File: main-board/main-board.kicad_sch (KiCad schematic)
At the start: 52 parts, among them J4 Conn_01x03_Pin, J5 COM, J6 Conn_01x03_Pin, SW1 SW_SPST, U1 ADA4898-2, U2 ADA4898-2, U3 AD633ANZ

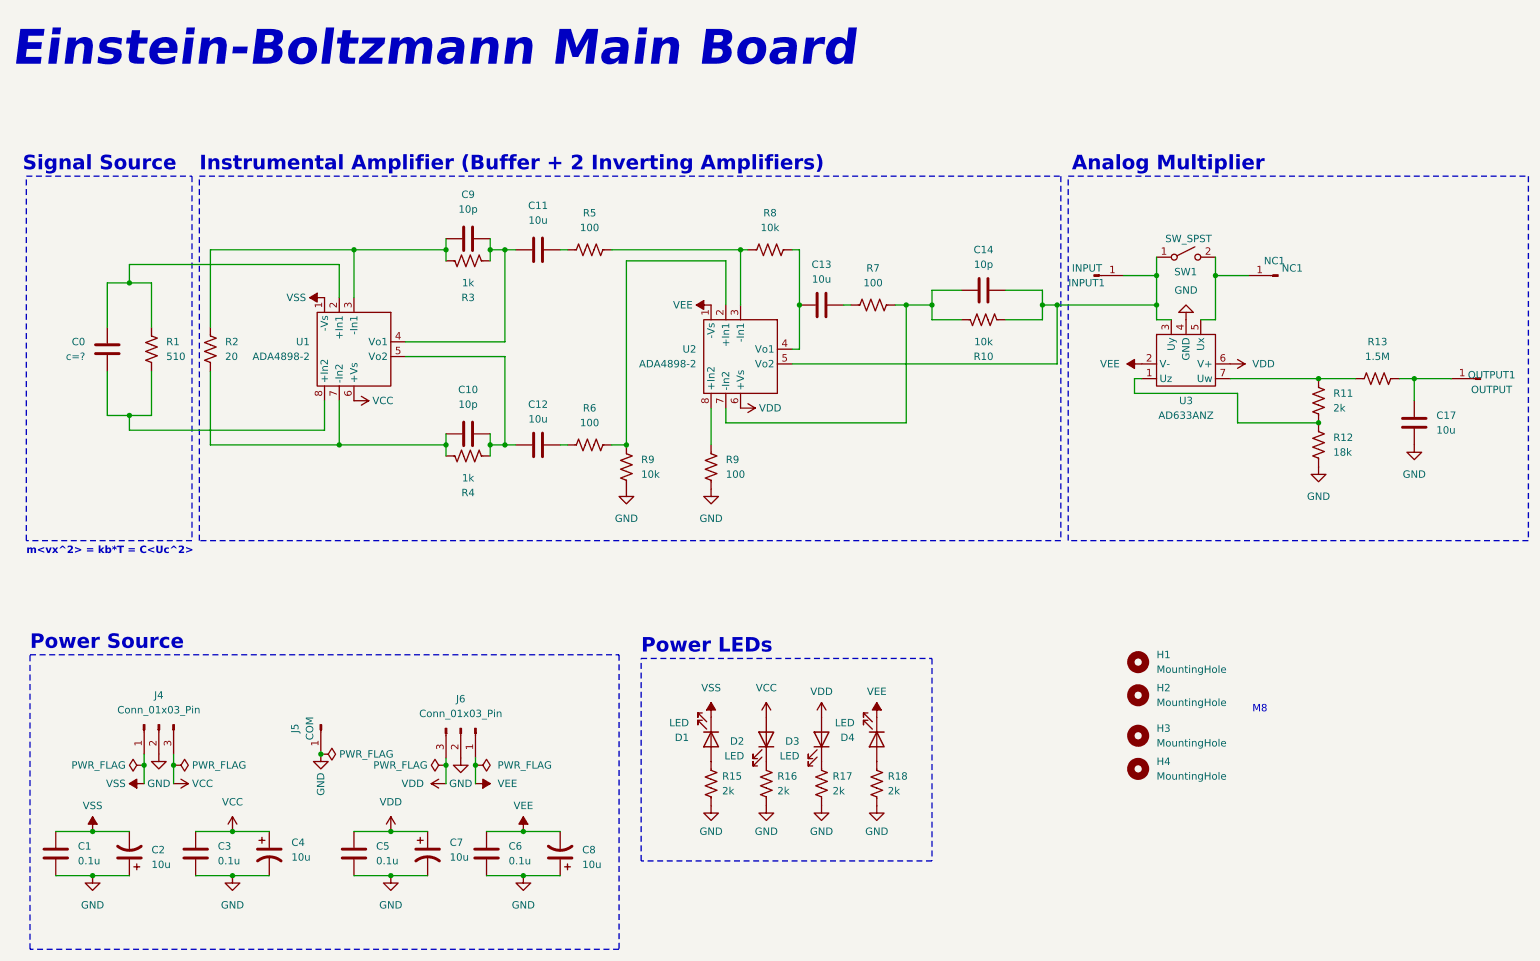
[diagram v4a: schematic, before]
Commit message: Modifies Main Board PCB Layout component disposal
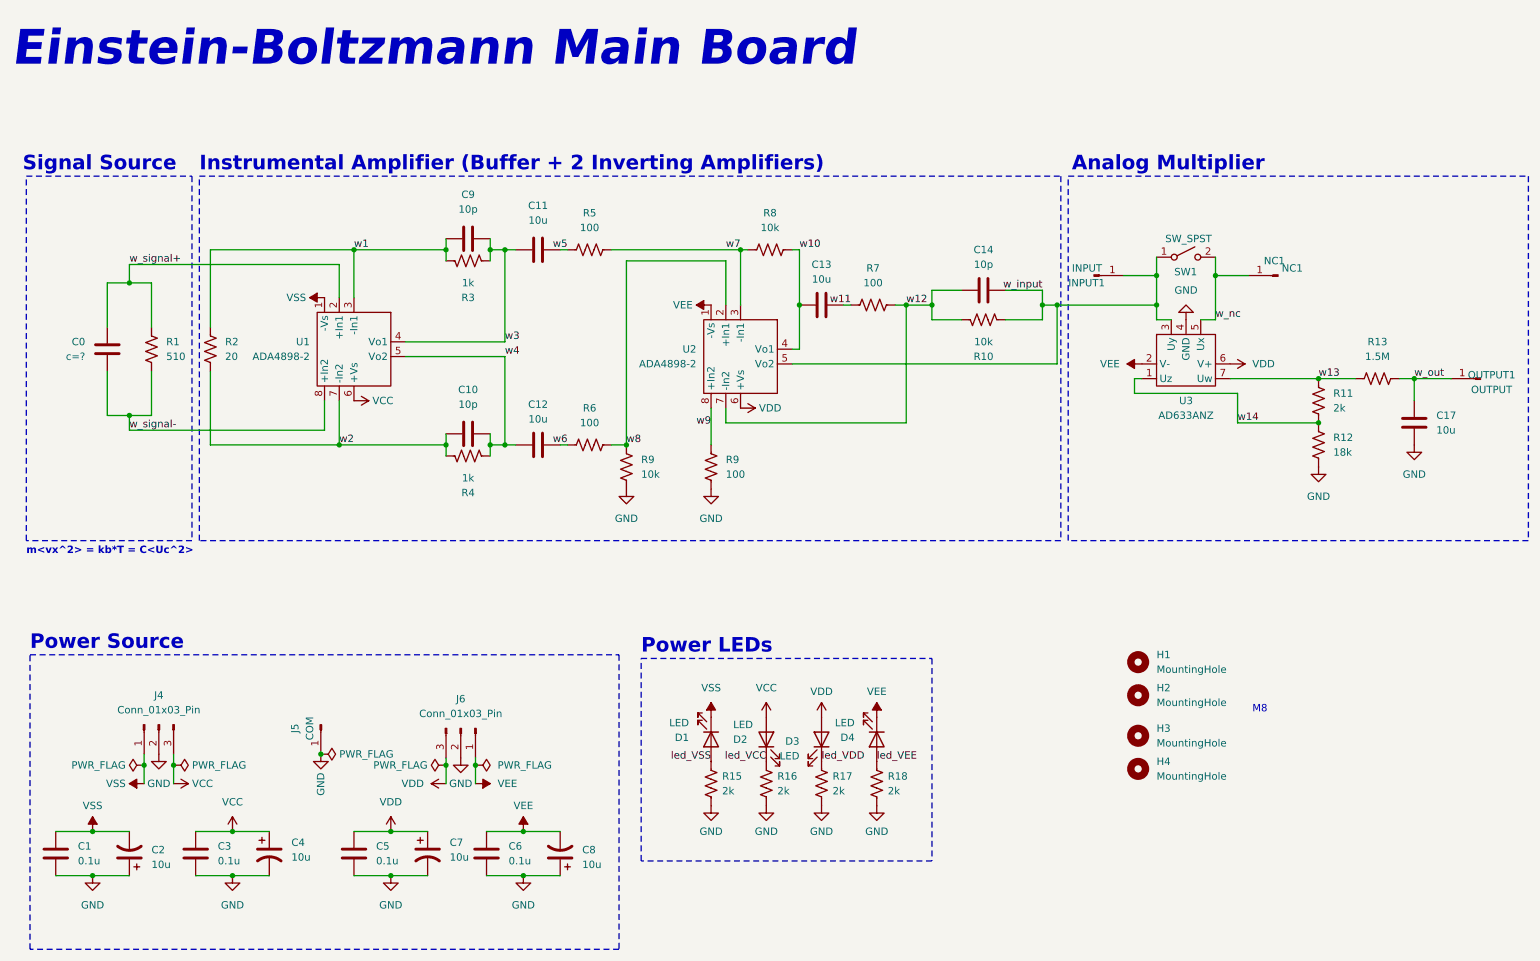
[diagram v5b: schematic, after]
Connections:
- net w_signal-: now reaches C0.1, R1.2, U1.8 (+In2)
- net w_signal+: now reaches C0.2, R1.1, U1.2 (+In1)
- net w5: now reaches C11.2, R5.1
- net w7: now reaches R5.2, R8.1, U2.3 (-In1)
- net w12: now reaches C14.1, R10.1, R7.2, U2.7 (-In2)
- net w_input: now reaches C14.2, INPUT1.1 (Pin_1), R10.2, SW1.1 (A), U2.5 (Vo2), U3.3 (Uy)
- net w10: now reaches C13.1, R8.2, U2.4 (Vo1)
- net w11: now reaches C13.2, R7.1
- net w4: now reaches C10.2, C12.1, R4.1, U1.5 (Vo2)
- net w2: now reaches C10.1, R2.2, R4.2, U1.7 (-In2)
- net led_VDD: now reaches D3.1 (K), R17.1
- net w1: now reaches C9.1, R2.1, R3.1, U1.3 (-In1)
- net w3: now reaches C11.1, C9.2, R3.2, U1.4 (Vo1)
- net w9: now reaches R9.2, U2.8 (+In2)
- net led_VSS: now reaches D1.2 (A), R15.1
- net w_nc: now reaches NC1.1 (Pin_1), SW1.2 (B), U3.5 (Ux)
- net w6: now reaches C12.2, R6.1
- net w8: now reaches R6.2, R9.2, U2.2 (+In1)
- net w14: now reaches R11.2, R12.1, U3.1 (Uz)
- net w_out: now reaches C17.1, OUTPUT1.1 (Pin_1), R13.2
- net led_VCC: now reaches D2.1 (K), R16.1
- net w13: now reaches R11.1, R13.1, U3.7 (Uw)
- net led_VEE: now reaches D4.2 (A), R18.1
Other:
- moved on the sheet: D2
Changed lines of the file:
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@@
     (effects (font (size 2.5 2.5) bold) (justify left bottom))
+  )
+  (label "w_input" (at 196.215 65.405 180) (fields_autoplaced)
+    (effects (font (size 1.27 1.27)) (justify right bottom))
+  )
+  (label "w_out" (at 260.35 80.645 0) (fields_autoplaced)
+    (effects (font (size 1.27 1.27)) (justify left bottom))
+  )
+  (label "w8" (at 124.46 92.075 0) (fields_autoplaced)
+    (effects (font (size 1.27 1.27)) (justify left bottom))
+  )
+  (label "led_VCC" (at 148.59 146.685 180) (fields_autoplaced)
+    (effects (font (size 1.27 1.27)) (justify right bottom))
+  )
+  (label "w6" (at 114.3 92.075 180) (fields_autoplaced)
+    (effects (font (size 1.27 1.27)) (justify right bottom))
+  )
+  (label "w3" (at 103.505 74.295 0) (fields_autoplaced)
+    (effects (font (size 1.27 1.27)) (justify left bottom))
+  )
+  (label "w14" (at 229.87 88.265 0) (fields_autoplaced)
+    (effects (font (size 1.27 1.27)) (justify left bottom))
+  )
+  (label "w_nc" (at 226.06 70.485 0) (fields_autoplaced)
+    (effects (font (size 1.27 1.27)) (justify left bottom))
+  )
+  (label "led_VSS" (at 139.065 146.685 180) (fields_autoplaced)
+    (effects (font (size 1.27 1.27)) (justify right bottom))
+  )
+  (label "w1" (at 77.47 58.42 0) (fields_autoplaced)
+    (effects (font (size 1.27 1.27)) (justify left bottom))
+  )
+  (label "w4" (at 103.505 76.835 0) (fields_autoplaced)
+    (effects (font (size 1.27 1.27)) (justify left bottom))
+  )
+  (label "led_VEE" (at 167.64 146.685 0) (fields_autoplaced)
+    (effects (font (size 1.27 1.27)) (justify left bottom))
+  )
+  (label "w7" (at 144.145 58.42 180) (fields_autoplaced)
+    (effects (font (size 1.27 1.27)) (justify right bottom))
+  )
+  (label "w5" (at 114.3 58.42 180) (fields_autoplaced)
+    (effects (font (size 1.27 1.27)) (justify right bottom))
+  )
+  (label "w13" (at 243.84 80.645 0) (fields_autoplaced)
+    (effects (font (size 1.27 1.27)) (justify left bottom))
+  )
+  (label "w10" (at 154.305 58.42 0) (fields_autoplaced)
+    (effects (font (size 1.27 1.27)) (justify left bottom))
+  )
+  (label "w11" (at 163.195 67.945 180) (fields_autoplaced)
+    (effects (font (size 1.27 1.27)) (justify right bottom))
+  )
+  (label "w_signal+" (at 38.735 60.96 0) (fields_autoplaced)
+    (effects (font (size 1.27 1.27)) (justify left bottom))
+  )
+  (label "w9" (at 139.065 88.9 180) (fields_autoplaced)
+    (effects (font (size 1.27 1.27)) (justify right bottom))
+  )
+  (label "w_signal-" (at 38.735 89.535 0) (fields_autoplaced)
+    (effects (font (size 1.27 1.27)) (justify left bottom))
+  )
+  (label "w12" (at 172.72 67.945 0) (fields_autoplaced)
+    (effects (font (size 1.27 1.27)) (justify left bottom))
+  )
+  (label "led_VDD" (at 158.115 146.685 0) (fields_autoplaced)
+    (effects (font (size 1.27 1.27)) (justify left bottom))
+  )
+  (label "w2" (at 74.93 92.075 0) (fields_autoplaced)
+    (effects (font (size 1.27 1.27)) (justify left bottom))
   )
   (symbol (lib_id "Device:C") (at 34.925 75.565 0) (mirror x) (unit 1)
@@
     )
   )
-  (symbol (lib_id "Device:LED") (at 148.59 142.875 270) (mirror x) (unit 1)
+  (symbol (lib_id "Device:LED") (at 148.59 142.875 90) (unit 1)
     (in_bom yes) (on_board yes) (dnp no)
-    (property "Reference" "D2" (at 144.78 143.1925 90)
-      (effects (font (size 1.27 1.27)) (justify right))
-    )
-    (property "Value" "LED" (at 144.78 145.7325 90)
-      (effects (font (size 1.27 1.27)) (justify right))
-    )
+    (property "Reference" "D2" (at 142.875 142.875 90)
+      (effects (font (size 1.27 1.27)) (justify right))
+    )
+    (property "Value" "LED" (at 142.875 140.335 90)
+      (effects (font (size 1.27 1.27)) (justify right))
+    )

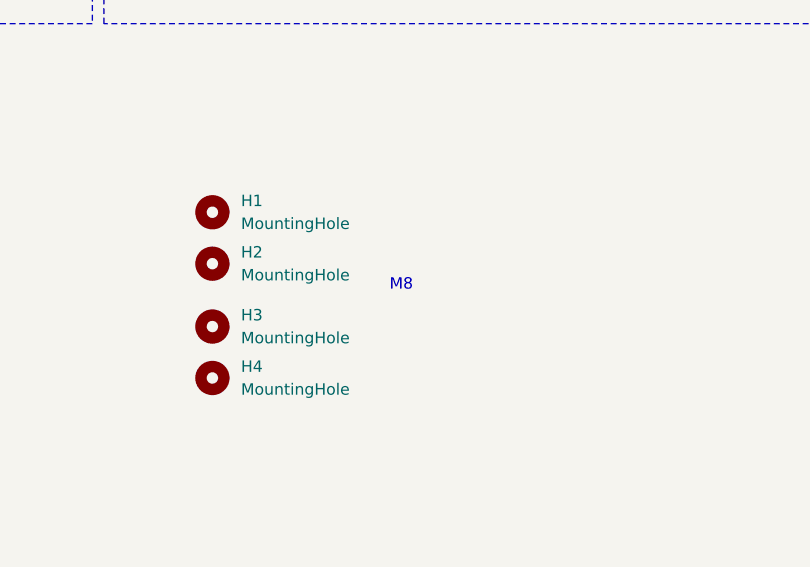
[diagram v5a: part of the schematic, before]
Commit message: Change M8 Holes to M5 Holes
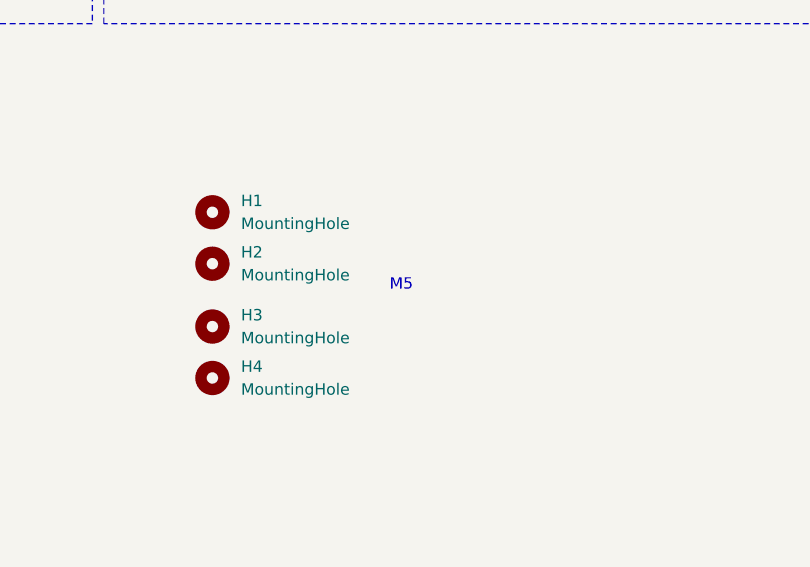
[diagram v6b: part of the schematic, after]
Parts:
- H1, H2, H3, H4: footprint MountingHole:MountingHole_8.4mm_M8 -> MountingHole:MountingHole_5.3mm_M5
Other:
- note added: "M5"
- note removed: "M8"
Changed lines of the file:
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@@
     (effects (font (size 2.5 2.5) bold) (justify left bottom))
   )
-  (text "M8" (at 232.41 138.43 0)
+  (text "M5" (at 232.41 138.43 0)
     (effects (font (size 1.27 1.27)) (justify left bottom))
   )
@@
       (effects (font (size 1.27 1.27)) (justify left))
     )
-    (property "Footprint" "MountingHole:MountingHole_8.4mm_M8" (at 212.725 129.54 0)
+    (property "Footprint" "MountingHole:MountingHole_5.3mm_M5" (at 212.725 129.54 0)
       (effects (font (size 1.27 1.27)) hide)
     )
@@
       (effects (font (size 1.27 1.27)) (justify left))
     )
-    (property "Footprint" "MountingHole:MountingHole_8.4mm_M8" (at 212.725 142.24 0)
+    (property "Footprint" "MountingHole:MountingHole_5.3mm_M5" (at 212.725 142.24 0)
       (effects (font (size 1.27 1.27)) hide)
     )
@@
       (effects (font (size 1.27 1.27)) (justify left))
     )
-    (property "Footprint" "MountingHole:MountingHole_8.4mm_M8" (at 212.725 135.255 0)
+    (property "Footprint" "MountingHole:MountingHole_5.3mm_M5" (at 212.725 135.255 0)
       (effects (font (size 1.27 1.27)) hide)
     )
@@
       (effects (font (size 1.27 1.27)) (justify left))
     )
-    (property "Footprint" "MountingHole:MountingHole_8.4mm_M8" (at 212.725 147.955 0)
-      (effects (font (size 1.27 1.27)) hide)
-    )
+    (property "Footprint" "MountingHole:MountingHole_5.3mm_M5" (at 212.725 147.955 0)
+      (effects (font (size 1.27 1.27)) hide)
+    )

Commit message: Changes capacitor and resistor footprints
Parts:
- C11, C12, C13, C17: footprint Capacitor_THT:C_Disc_D6.0mm_W2.5mm_P5.00mm -> Capacitor_THT:C_Rect_L24.0mm_W8.6mm_P22.50mm_MKT
- R1, R10, R11, R12, R13, R15, R16, R17, R18, R2, R3, R4, R5, R6, R7, R8, R9: footprint Resistor_THT:R_Axial_DIN0207_L6.3mm_D2.5mm_P15.24mm_Horizontal -> Resistor_THT:R_Axial_DIN0207_L6.3mm_D2.5mm_P7.62mm_Horizontal
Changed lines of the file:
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@@
       (effects (font (size 1.27 1.27)))
     )
-    (property "Footprint" "Resistor_THT:R_Axial_DIN0207_L6.3mm_D2.5mm_P15.24mm_Horizontal" (at 118.364 57.404 90)
+    (property "Footprint" "Resistor_THT:R_Axial_DIN0207_L6.3mm_D2.5mm_P7.62mm_Horizontal" (at 118.364 57.404 90)
       (effects (font (size 1.27 1.27)) hide)
     )
@@
       (effects (font (size 1.27 1.27)))
     )
-    (property "Footprint" "Capacitor_THT:C_Disc_D6.0mm_W2.5mm_P5.00mm" (at 161.925 66.9798 0)
+    (property "Footprint" "Capacitor_THT:C_Rect_L24.0mm_W8.6mm_P22.50mm_MKT" (at 161.925 66.9798 0)
       (effects (font (size 1.27 1.27)) hide)
     )
@@
       (effects (font (size 1.27 1.27)))
     )
-    (property "Footprint" "Resistor_THT:R_Axial_DIN0207_L6.3mm_D2.5mm_P15.24mm_Horizontal" (at 96.901 92.964 90)
+    (property "Footprint" "Resistor_THT:R_Axial_DIN0207_L6.3mm_D2.5mm_P7.62mm_Horizontal" (at 96.901 92.964 90)
       (effects (font (size 1.27 1.27)) hide)
     )
@@
       (effects (font (size 1.27 1.27)))
     )
-    (property "Footprint" "Resistor_THT:R_Axial_DIN0207_L6.3mm_D2.5mm_P15.24mm_Horizontal" (at 186.309 71.501 90)
+    (property "Footprint" "Resistor_THT:R_Axial_DIN0207_L6.3mm_D2.5mm_P7.62mm_Horizontal" (at 186.309 71.501 90)
       (effects (font (size 1.27 1.27)) hide)
     )
@@
       (effects (font (size 1.27 1.27)))
     )
-    (property "Footprint" "Capacitor_THT:C_Disc_D6.0mm_W2.5mm_P5.00mm" (at 113.03 57.4548 0)
+    (property "Footprint" "Capacitor_THT:C_Rect_L24.0mm_W8.6mm_P22.50mm_MKT" (at 113.03 57.4548 0)
       (effects (font (size 1.27 1.27)) hide)
     )
@@
       (effects (font (size 1.27 1.27)) (justify right))
     )
-    (property "Footprint" "Resistor_THT:R_Axial_DIN0207_L6.3mm_D2.5mm_P15.24mm_Horizontal" (at 138.049 95.631 90)
+    (property "Footprint" "Resistor_THT:R_Axial_DIN0207_L6.3mm_D2.5mm_P7.62mm_Horizontal" (at 138.049 95.631 90)
       (effects (font (size 1.27 1.27)) hide)
     )
@@
       (effects (font (size 1.27 1.27)))
     )
-    (property "Footprint" "Capacitor_THT:C_Disc_D6.0mm_W2.5mm_P5.00mm" (at 113.03 91.1098 0)
+    (property "Footprint" "Capacitor_THT:C_Rect_L24.0mm_W8.6mm_P22.50mm_MKT" (at 113.03 91.1098 0)
       (effects (font (size 1.27 1.27)) hide)
     )
@@
       (effects (font (size 1.27 1.27)))
     )
-    (property "Footprint" "Resistor_THT:R_Axial_DIN0207_L6.3mm_D2.5mm_P15.24mm_Horizontal" (at 118.364 91.059 90)
+    (property "Footprint" "Resistor_THT:R_Axial_DIN0207_L6.3mm_D2.5mm_P7.62mm_Horizontal" (at 118.364 91.059 90)
       (effects (font (size 1.27 1.27)) hide)
     )
@@
       (effects (font (size 1.27 1.27)))
     )
-    (property "Footprint" "Resistor_THT:R_Axial_DIN0207_L6.3mm_D2.5mm_P15.24mm_Horizontal" (at 167.259 66.929 90)
+    (property "Footprint" "Resistor_THT:R_Axial_DIN0207_L6.3mm_D2.5mm_P7.62mm_Horizontal" (at 167.259 66.929 90)
       (effects (font (size 1.27 1.27)) hide)
     )
@@
       (effects (font (size 1.27 1.27)) (justify left))
     )
-    (property "Footprint" "Resistor_THT:R_Axial_DIN0207_L6.3mm_D2.5mm_P15.24mm_Horizontal" (at 244.856 92.329 90)
+    (property "Footprint" "Resistor_THT:R_Axial_DIN0207_L6.3mm_D2.5mm_P7.62mm_Horizontal" (at 244.856 92.329 90)
       (effects (font (size 1.27 1.27)) hide)
     )
@@
       (effects (font (size 1.27 1.27)) (justify left))
     )
-    (property "Footprint" "Capacitor_THT:C_Disc_D6.0mm_W2.5mm_P5.00mm" (at 261.3152 92.075 0)
+    (property "Footprint" "Capacitor_THT:C_Rect_L24.0mm_W8.6mm_P22.50mm_MKT" (at 261.3152 92.075 0)
       (effects (font (size 1.27 1.27)) hide)
     )
@@
       (effects (font (size 1.27 1.27)) (justify left))
     )
-    (property "Footprint" "Resistor_THT:R_Axial_DIN0207_L6.3mm_D2.5mm_P15.24mm_Horizontal" (at 244.856 84.709 90)
+    (property "Footprint" "Resistor_THT:R_Axial_DIN0207_L6.3mm_D2.5mm_P7.62mm_Horizontal" (at 244.856 84.709 90)
       (effects (font (size 1.27 1.27)) hide)
     )
@@
       (effects (font (size 1.27 1.27)) (justify left))
     )
-    (property "Footprint" "Resistor_THT:R_Axial_DIN0207_L6.3mm_D2.5mm_P15.24mm_Horizontal" (at 149.606 150.749 90)
+    (property "Footprint" "Resistor_THT:R_Axial_DIN0207_L6.3mm_D2.5mm_P7.62mm_Horizontal" (at 149.606 150.749 90)
       (effects (font (size 1.27 1.27)) hide)
     )
@@
       (effects (font (size 1.27 1.27)) (justify left))
     )
-    (property "Footprint" "Resistor_THT:R_Axial_DIN0207_L6.3mm_D2.5mm_P15.24mm_Horizontal" (at 168.656 150.749 90)
+    (property "Footprint" "Resistor_THT:R_Axial_DIN0207_L6.3mm_D2.5mm_P7.62mm_Horizontal" (at 168.656 150.749 90)
       (effects (font (size 1.27 1.27)) hide)
     )
@@
       (effects (font (size 1.27 1.27)))
     )
-    (property "Footprint" "Resistor_THT:R_Axial_DIN0207_L6.3mm_D2.5mm_P15.24mm_Horizontal" (at 254.254 79.629 90)
+    (property "Footprint" "Resistor_THT:R_Axial_DIN0207_L6.3mm_D2.5mm_P7.62mm_Horizontal" (at 254.254 79.629 90)
       (effects (font (size 1.27 1.27)) hide)
     )
@@
       (effects (font (size 1.27 1.27)) (justify left))
     )
-    (property "Footprint" "Resistor_THT:R_Axial_DIN0207_L6.3mm_D2.5mm_P15.24mm_Horizontal" (at 159.131 150.749 90)
+    (property "Footprint" "Resistor_THT:R_Axial_DIN0207_L6.3mm_D2.5mm_P7.62mm_Horizontal" (at 159.131 150.749 90)
       (effects (font (size 1.27 1.27)) hide)
     )
@@
       (effects (font (size 1.27 1.27)) (justify left))
     )
-    (property "Footprint" "Resistor_THT:R_Axial_DIN0207_L6.3mm_D2.5mm_P15.24mm_Horizontal" (at 53.721 75.819 90)
+    (property "Footprint" "Resistor_THT:R_Axial_DIN0207_L6.3mm_D2.5mm_P7.62mm_Horizontal" (at 53.721 75.819 90)
       (effects (font (size 1.27 1.27)) hide)
     )
@@
       (effects (font (size 1.27 1.27)) (justify left))
     )
-    (property "Footprint" "Resistor_THT:R_Axial_DIN0207_L6.3mm_D2.5mm_P15.24mm_Horizontal" (at 43.561 75.819 90)
+    (property "Footprint" "Resistor_THT:R_Axial_DIN0207_L6.3mm_D2.5mm_P7.62mm_Horizontal" (at 43.561 75.819 90)
       (effects (font (size 1.27 1.27)) hide)
     )
@@
       (effects (font (size 1.27 1.27)))
     )
-    (property "Footprint" "Resistor_THT:R_Axial_DIN0207_L6.3mm_D2.5mm_P15.24mm_Horizontal" (at 97.409 61.341 90)
+    (property "Footprint" "Resistor_THT:R_Axial_DIN0207_L6.3mm_D2.5mm_P7.62mm_Horizontal" (at 97.409 61.341 90)
       (effects (font (size 1.27 1.27)) hide)
     )
@@
       (effects (font (size 1.27 1.27)))
     )
-    (property "Footprint" "Resistor_THT:R_Axial_DIN0207_L6.3mm_D2.5mm_P15.24mm_Horizontal" (at 149.479 57.404 90)
+    (property "Footprint" "Resistor_THT:R_Axial_DIN0207_L6.3mm_D2.5mm_P7.62mm_Horizontal" (at 149.479 57.404 90)
       (effects (font (size 1.27 1.27)) hide)
     )
@@
       (effects (font (size 1.27 1.27)) (justify right))
     )
-    (property "Footprint" "Resistor_THT:R_Axial_DIN0207_L6.3mm_D2.5mm_P15.24mm_Horizontal" (at 123.444 95.631 90)
+    (property "Footprint" "Resistor_THT:R_Axial_DIN0207_L6.3mm_D2.5mm_P7.62mm_Horizontal" (at 123.444 95.631 90)
       (effects (font (size 1.27 1.27)) hide)
     )
@@
       (effects (font (size 1.27 1.27)) (justify left))
     )
-    (property "Footprint" "Resistor_THT:R_Axial_DIN0207_L6.3mm_D2.5mm_P15.24mm_Horizontal" (at 140.081 150.749 90)
-      (effects (font (size 1.27 1.27)) hide)
-    )
+    (property "Footprint" "Resistor_THT:R_Axial_DIN0207_L6.3mm_D2.5mm_P7.62mm_Horizontal" (at 140.081 150.749 90)
+      (effects (font (size 1.27 1.27)) hide)
+    )
